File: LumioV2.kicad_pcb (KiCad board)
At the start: 2 copper layers, 79 parts, among them J1 I2C POINT 1 - QWIIC, J10 MOTOR B, J11 Analog Input, J12 Analog Input, J13 Analog Input, J14 Analog Input, J15 Analog Input, J16 Analog Input, J17 Analog Input, J18 Analog Input, J19 Serial Pads, J2 I2C POINT 2 - QWIIC, J20 Conn_02x13_Odd_Even, J21 Conn_02x02_Odd_Even, J3 I2C POINT 3 - JST-PH, J4 I2C POINT 4 - JST-PH, J5 Raspi 5, J6 US Dist - Front, J7 US Dist - Back, J8 USB_C_Receptacle_USB2.0_14P, J9 MOTOR A, SW1 SW_Push, SW2 SW_Push, U1 LM2577T-ADJ/NOPB, U2 L298N, U3 MCP3008, U4 RP2040, U5 W25Q64JVXGIQ TR, Y1 Crystal

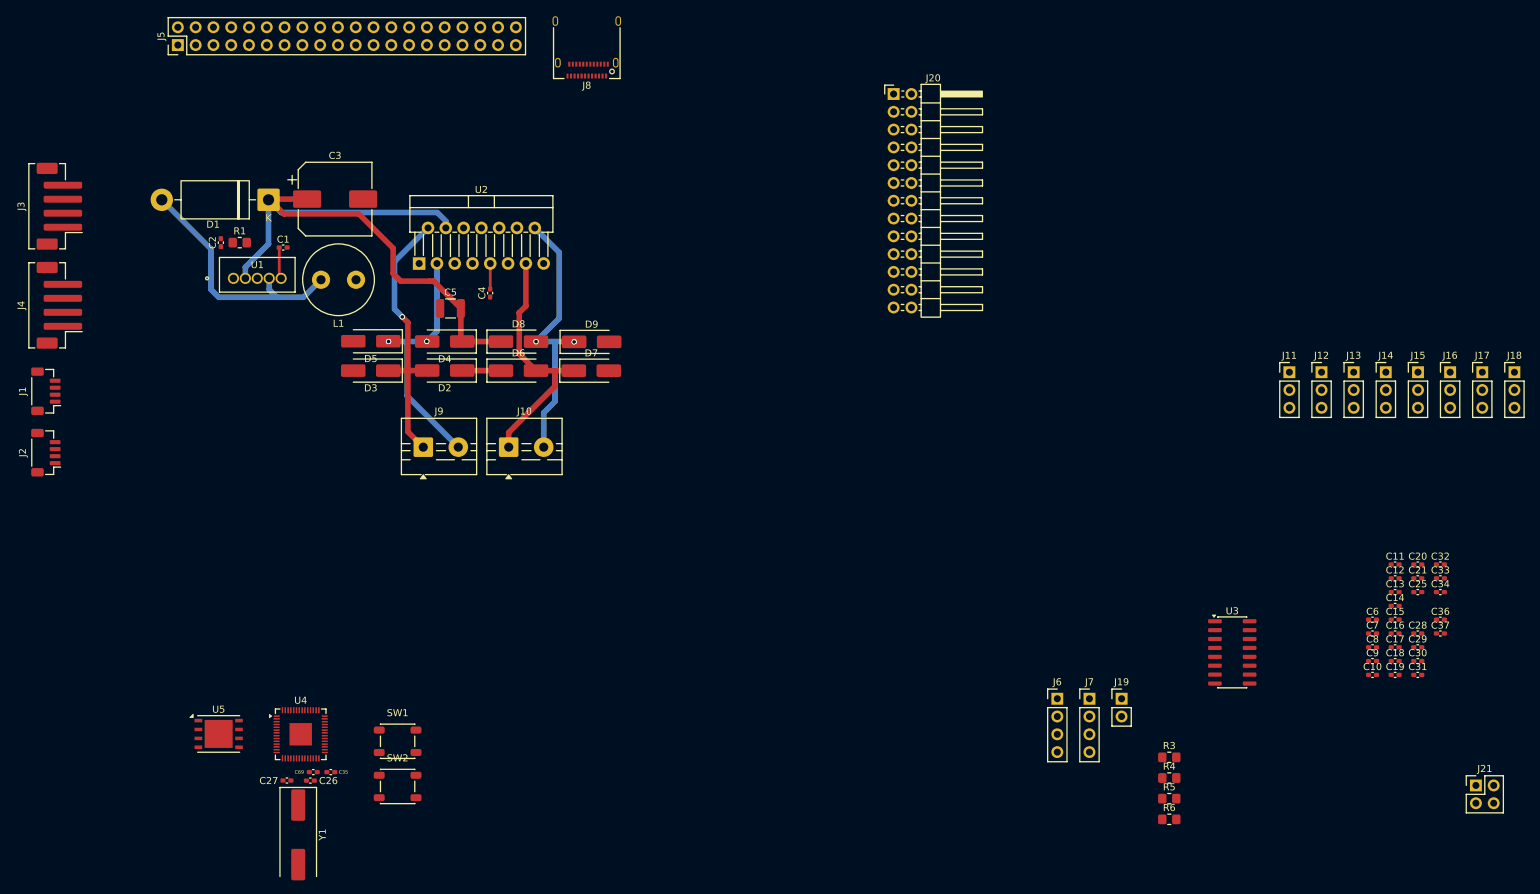
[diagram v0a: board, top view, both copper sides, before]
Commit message: routed abit; replaced the MCP3008 footprint to a 16 pin socket, so that i can swap it easily if the user fries it somehow
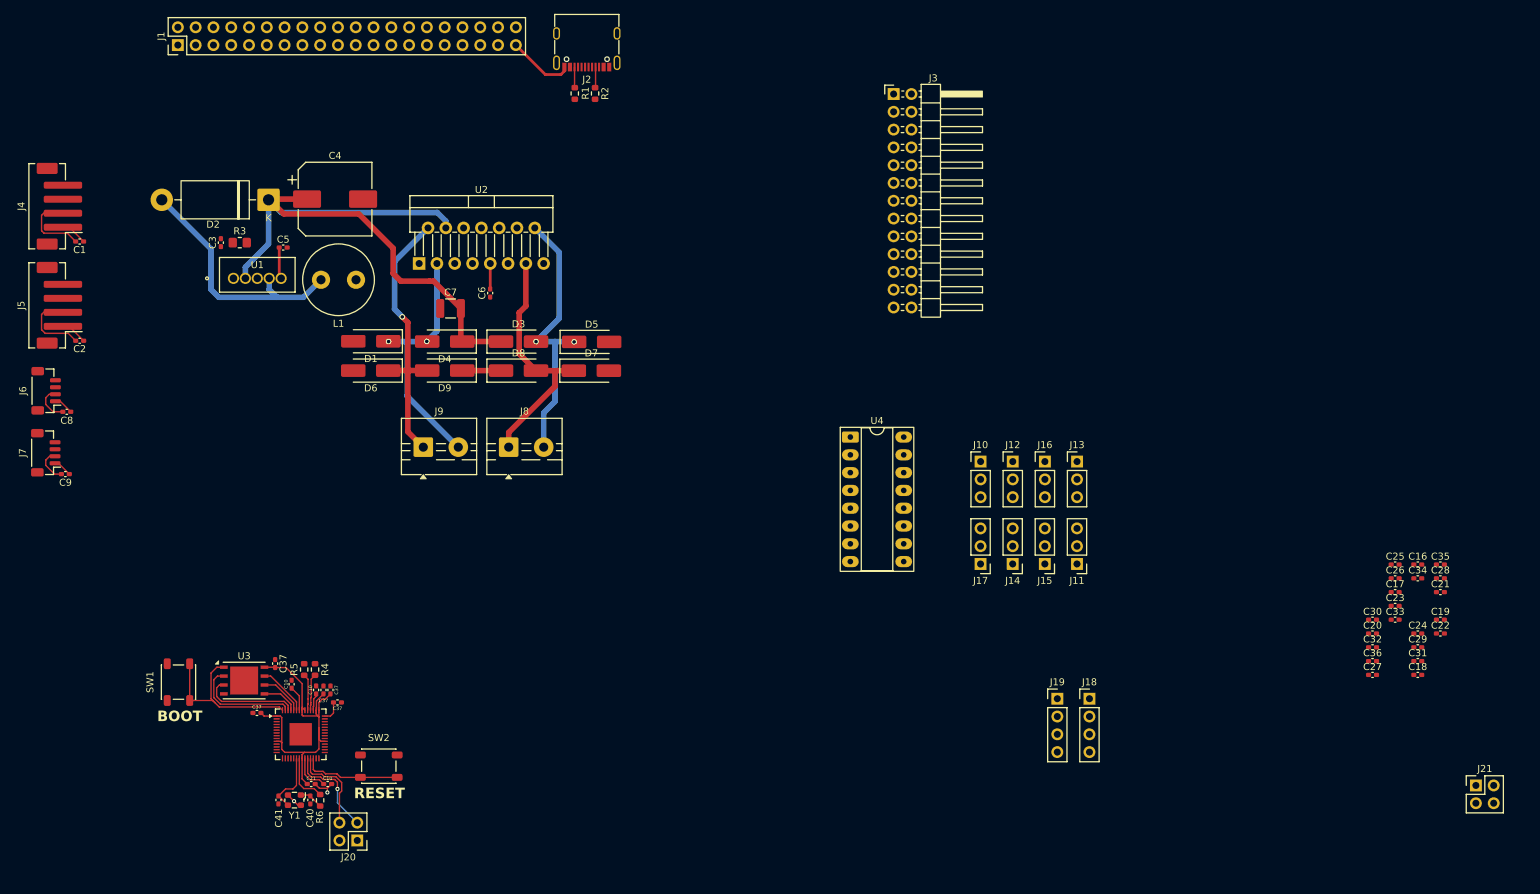
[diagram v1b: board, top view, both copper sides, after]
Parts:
- removed the J19 at (214.7, 137.9)
- removed the J2 at (61.1, 102.8)
- added C10: 1uF, Capacitor_SMD:C_0402_1005Metric_Pad0.74x0.62mm_HandSolder, F.Cu at (99.7, 136.7)
- added C10: 1uF, Capacitor_SMD:C_0402_1005Metric_Pad0.74x0.62mm_HandSolder, F.Cu at (96.2, 135.8)
- added C37: 100nF, Capacitor_SMD:C_0402_1005Metric_Pad0.74x0.62mm_HandSolder, F.Cu at (101.8, 136.7)
- added C37: 100nF, Capacitor_SMD:C_0402_1005Metric_Pad0.74x0.62mm_HandSolder, F.Cu at (91.2, 139.9)
- added C37: 100nF, Capacitor_SMD:C_0402_1005Metric_Pad0.74x0.62mm_HandSolder, F.Cu at (102.8, 138.4)
- added C37: 100nF, Capacitor_SMD:C_0402_1005Metric_Pad0.74x0.62mm_HandSolder, F.Cu at (100.8, 136.7)
- added J20: Header programmer, Connector_PinHeader_2.54mm:PinHeader_2x02_P2.54mm_Vertical, F.Cu at (105.6, 158.2)
- added J6: I2C POINT 2 - QWIIC, Connector_JST:JST_SH_BM04B-SRSS-TB_1x04-1MP_P1.00mm_Vertical, F.Cu at (61.1, 94.0)
- added R6: 1K, Resistor_SMD:R_0603_1608Metric, F.Cu at (100.3, 152.4)
- C40: renamed from C26; value 33pF -> 15pF
- C41: renamed from C27; value 33pF -> 15pF
- J2: renamed from J8; footprint Connector_USB:USB_C_Receptacle_Amphenol_12401610E4-2A -> Connector_USB:USB_C_Receptacle_G-Switch_GT-USB-7010ASV
- R1: renamed from R6; footprint Resistor_SMD:R_0805_2012Metric_Pad1.20x1.40mm_HandSolder -> Resistor_SMD:R_0603_1608Metric
- R2: renamed from R5; footprint Resistor_SMD:R_0805_2012Metric_Pad1.20x1.40mm_HandSolder -> Resistor_SMD:R_0603_1608Metric
- R4: renamed from R3; footprint Resistor_SMD:R_0805_2012Metric_Pad1.20x1.40mm_HandSolder -> Resistor_SMD:R_0603_1608Metric
- R5: renamed from R4; footprint Resistor_SMD:R_0805_2012Metric_Pad1.20x1.40mm_HandSolder -> Resistor_SMD:R_0603_1608Metric
- U4: renamed from U3; footprint Package_SO:SOIC-16_3.9x9.9mm_P1.27mm -> Package_DIP:DIP-16_W7.62mm_Socket_LongPads
- Y1: value Crystal -> ECS-2520MV-xxx-xx; footprint Crystal:Crystal_SMD_HC49-SD -> Oscillator:Oscillator_SMD_ECS_2520MV-xxx-xx-4Pin_2.5x2.0mm
- moved C1 197.8 mm to (65.9, 72.6), turned to 180 degrees
- moved C2 193.3 mm to (65.9, 86.8), turned to 180 degrees
- moved C8 192.3 mm to (64.1, 97.0), turned to 180 degrees
- moved C9 191.5 mm to (63.9, 105.8), turned to 180 degrees
- moved C37 163.5 mm to (93.8, 132.9), turned to -90 degrees
- moved R1 134.0 mm to (136.6, 51.5), turned to 90 degrees
- moved R2 129.8 mm to (139.5, 51.5), turned to -90 degrees
- moved R5 124.5 mm to (98.0, 133.8), turned to 90 degrees
- moved R4 122.6 mm to (99.5, 133.8), turned to -90 degrees
- moved J17 81.0 mm to (194.6, 118.7), turned to 180 degrees
- moved J14 72.4 mm to (199.2, 118.7), turned to 180 degrees
- moved J15 64.0 mm to (203.8, 118.7), turned to 180 degrees
- moved U4 62.6 mm to (176.0, 100.6)
- moved J11 55.9 mm to (208.3, 118.7), turned to 180 degrees
- moved J12 45.9 mm to (199.2, 104.1)
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- renumbered C19 to C1, C35 to C10, C20 to C16, C13 to C17, C31 to C18, C36 to C19, C18 to C2, C7 to C20, C34 to C21, C69 to C21, C37 to C22, C14 to C23, C28 to C24, C11 to C25, C12 to C26, C10 to C27, C33 to C28, C2 to C3, C6 to C30, C30 to C31, C8 to C32, C15 to C33, C21 to C34, C32 to C35, C9 to C36, C25 to C37, C3 to C4, C1 to C5, C4 to C6, C5 to C7, C16 to C8, C17 to C9, D5 to D1, D1 to D2, D8 to D3, D9 to D5, D3 to D6, D6 to D8, D2 to D9, J5 to J1, J11 to J10, J15 to J11, J14 to J13, J17 to J14, J16 to J15, J13 to J16, J18 to J17, J7 to J18, J6 to J19, J20 to J3, J3 to J5, J1 to J7, J10 to J8, R1 to R3, SW2 to SW1, SW1 to SW2, U5 to U3, U4 to U5
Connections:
- C37 pad 2: Net-(U5-VCC) -> +3V3
- C40 pad 2: Net-(U4-XOUT) -> Net-(Y1-Tri-State)
- C41 pad 1: Net-(U4-XIN) -> Net-(U5-XIN)
- J1 pad 18: unconnected-(J5-Pin_18-Pad18) -> Net-(J1-Pin_18)
- J1 pad 22: unconnected-(J5-Pin_22-Pad22) -> Net-(J1-Pin_22)
- U3 pad 8: Net-(U5-VCC) -> +3V3
- U5 pad 20: Net-(U4-XIN) -> Net-(U5-XIN)
- U5 pad 21: Net-(U4-XOUT) -> Net-(U5-XOUT)
- Y1 pad 1: Net-(U4-XOUT) -> Net-(Y1-Tri-State)
- Y1 pad 2: Net-(U4-XIN) -> GND
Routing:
- net +3V3: track 0.00 -> 83.8 mm
- net GND: track 0.00 -> 28.5 mm, vias 0 -> 2
- net Net-(U3-/CS): track 0.00 -> 25.7 mm
- net Net-(U3-DO_(IO1)): track 0.00 -> 15.5 mm
- net Net-(U5-RUN): track 0.00 -> 14.0 mm
- net Net-(U3-/WP_(IO2)): track 0.00 -> 13.9 mm
- net Net-(J20-Pin_3): track 0.00 -> 13.9 mm, vias 0 -> 1
- net Net-(J20-Pin_4): track 0.00 -> 12.9 mm
- net +1V1: track 0.00 -> 11.6 mm
- net Net-(U5-XIN): track 0.00 -> 8.96 mm
- net Net-(U3-/HOLD_or_/RESET_(IO3)): track 0.00 -> 7.29 mm
- net Net-(U5-XOUT): track 0.00 -> 7.26 mm
- net Net-(U3-CLK): track 0.00 -> 6.27 mm
- net Net-(U5-USB_DM): track 0.00 -> 5.26 mm
- net Net-(U3-DI_(IO0)): track 0.00 -> 5.25 mm
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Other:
- board text added: "BOOT"
- board text added: "RESET"
